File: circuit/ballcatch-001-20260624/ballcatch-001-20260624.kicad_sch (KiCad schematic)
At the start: 5 parts, among them J1 Conn_01x03_Pin, Q1 Q_Photo_NPN_CE

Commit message: Update VCC->+3.3V
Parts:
- J1: footprint (none) -> Connector_PinHeader_2.54mm:PinHeader_1x03_P2.54mm_Vertical
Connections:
- net VCC renamed +3.3V

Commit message: Update ボール補足センサのフットプリント紐づけ
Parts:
- D1: footprint (none) -> LED_THT:LED_D3.0mm
- Q1: footprint (none) -> @Thrive_footprint_ballcatch:NJL7502L
- R1, R2: footprint (none) -> Resistor_SMD:R_0603_1608Metric
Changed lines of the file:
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@@
 			)
 		)
-		(property "Footprint" ""
+		(property "Footprint" "Resistor_SMD:R_0603_1608Metric"
 			(at 93.98 61.468 90)
 			(hide yes)
@@
 			)
 		)
-		(property "Footprint" ""
+		(property "Footprint" "@Thrive_footprint_ballcatch:NJL7502L"
 			(at 102.87 64.77 0)
 			(hide yes)
@@
 			)
 		)
-		(property "Footprint" ""
+		(property "Footprint" "Resistor_SMD:R_0603_1608Metric"
 			(at 102.108 81.28 90)
 			(hide yes)
@@
 		(dnp no)
 		(fields_autoplaced yes)
-		(property "Reference" "#PWR03"
+		(property "Reference" "#PWR02"
 			(at 100.33 59.69 0)
 			(hide yes)
@@
 			(project "ballcatch-001-20260624"
 				(path "/6c5d531b-b83d-412d-92d2-0b817b08e392"
-					(reference "#PWR03")
+					(reference "#PWR02")
 					(unit 1)
 				)
@@
 		(dnp no)
 		(fields_autoplaced yes)
-		(property "Reference" "#PWR02"
+		(property "Reference" "#PWR04"
 			(at 149.86 73.66 0)
 			(hide yes)
@@
 			(project "ballcatch-001-20260624"
 				(path "/6c5d531b-b83d-412d-92d2-0b817b08e392"
-					(reference "#PWR02")
+					(reference "#PWR04")
 					(unit 1)
 				)
@@
 			)
 		)
-		(property "Footprint" ""
+		(property "Footprint" "LED_THT:LED_D3.0mm"
 			(at 82.55 59.69 0)
 			(hide yes)
@@
 		(dnp no)
 		(fields_autoplaced yes)
-		(property "Reference" "#PWR04"
+		(property "Reference" "#PWR01"
 			(at 76.2 97.79 0)
 			(hide yes)
@@
 			(project "ballcatch-001-20260624"
 				(path "/6c5d531b-b83d-412d-92d2-0b817b08e392"
-					(reference "#PWR04")
+					(reference "#PWR01")
 					(unit 1)
 				)
@@
 		(dnp no)
 		(fields_autoplaced yes)
-		(property "Reference" "#PWR01"
+		(property "Reference" "#PWR03"
 			(at 149.86 63.5 0)
 			(hide yes)
@@
 			(project "ballcatch-001-20260624"
 				(path "/6c5d531b-b83d-412d-92d2-0b817b08e392"
-					(reference "#PWR01")
-					(unit 1)
-				)
+					(reference "#PWR03")
+					(unit 1)
+				)

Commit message: Create 供給基板の回路図完成
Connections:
- net signal renamed BallCatch_{Back}
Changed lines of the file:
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@@
 		)
 	)
-	(global_label "signal"
+	(global_label "BallCatch_{Back}"
 		(shape input)
 		(at 135.89 59.69 0)
@@
 		)
 		(property "Intersheetrefs" "${INTERSHEET_REFS}"
-			(at 144.6203 59.69 0)
+			(at 148.7822 59.69 0)
 			(hide yes)
 			(show_name no)
@@
 		)
 	)
-	(global_label "signal"
+	(global_label "BallCatch_{Back}"
 		(shape output)
 		(at 92.71 74.93 180)
@@
 		)
 		(property "Intersheetrefs" "${INTERSHEET_REFS}"
-			(at 83.9797 74.93 0)
+			(at 79.8178 74.93 0)
 			(hide yes)
 			(show_name no)

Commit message: Update ボール補足センサのDR完了、JLCPCBのロゴ追加
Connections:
- net GND: now also D1.2 (K); no longer D1.1 (K)
- net at R1.1: now also D1.1 (A); no longer D1.2 (A)

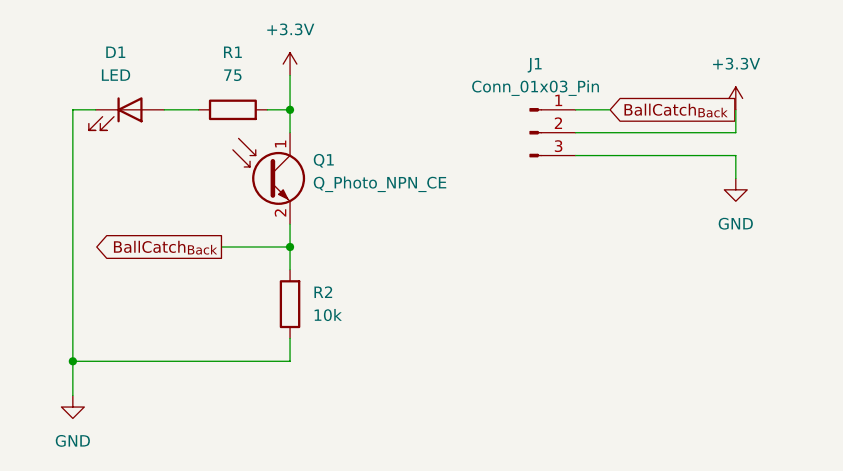
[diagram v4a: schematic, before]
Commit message: Update ボール補足基板のボード図を完成させた
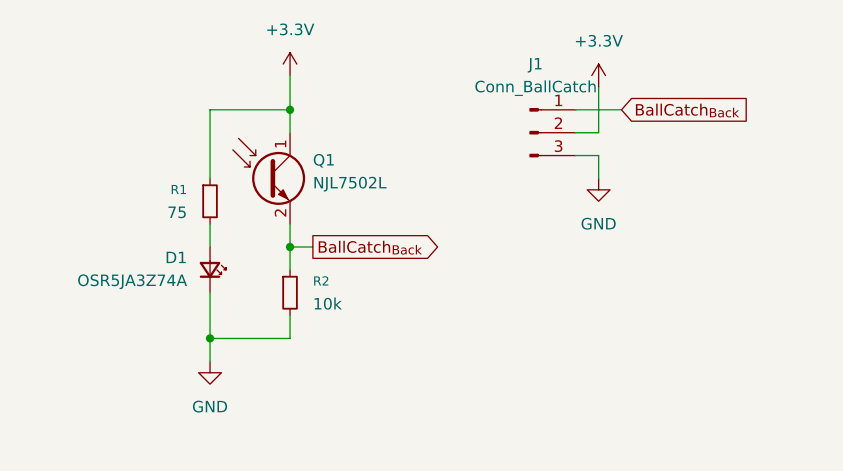
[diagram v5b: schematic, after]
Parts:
- removed D1: LED, LED_THT:LED_D3.0mm, symbol Device:LED
- removed R1: 75, Resistor_SMD:R_0603_1608Metric, symbol Device:R
- removed R2: 10k, Resistor_SMD:R_0603_1608Metric, symbol Device:R
- added D1: OSR5JA3Z74A, LED_THT:LED_D3.0mm, symbol Device:LED_Small
- added R1: 75, Resistor_THT:R_Axial_DIN0207_L6.3mm_D2.5mm_P7.62mm_Horizontal, symbol Device:R_Small
- added R2: 10k, Resistor_THT:R_Axial_DIN0207_L6.3mm_D2.5mm_P7.62mm_Horizontal, symbol Device:R_Small
- J1: value Conn_01x03_Pin -> Conn_BallCatch
- Q1: value Q_Photo_NPN_CE -> NJL7502L
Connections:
- net +3.3V: now also R1.1
- net BallCatch_{Back}: now also R2.1
- net GND: now also D1.2 (K), R2.2
- new net: D1.1 (A), R1.2
